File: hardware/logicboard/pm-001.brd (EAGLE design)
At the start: 45 x 45 mm, 18 parts, among them K1 G5V1, T1 2SC1815

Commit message: OSHW logo.
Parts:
- added LOGO1: OSHW-LOGOL-COPPER, SparkFun-Aesthetics:OSHW-LOGO-L_COPPER
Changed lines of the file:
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@@
 <setting verticaltext="up"/>
 </settings>
-<grid distance="50" unitdist="mil" unit="mil" style="lines" multiple="1" display="yes" altdistance="5" altunitdist="mil" altunit="mil"/>
+<grid distance="1" unitdist="mm" unit="mm" style="lines" multiple="1" display="yes" altdistance="5" altunitdist="mil" altunit="mil"/>
 <layers>
 <layer number="1" name="Top" color="4" fill="1" visible="no" active="yes"/>
-<layer number="16" name="Bottom" color="1" fill="1" visible="no" active="yes"/>
+<layer number="16" name="Bottom" color="1" fill="1" visible="yes" active="yes"/>
 <layer number="17" name="Pads" color="2" fill="1" visible="yes" active="yes"/>
 <layer number="18" name="Vias" color="2" fill="1" visible="yes" active="yes"/>
@@
 <attribute name="VALUE" x="36.47" y="43.455" size="1.27" layer="27" rot="R180"/>
 </element>
+<element name="LOGO1" library="SparkFun-Aesthetics" package="OSHW-LOGO-L_COPPER" value="OSHW-LOGOL-COPPER" x="22.5" y="15" rot="MR0"/>
 </elements>
 <signals>

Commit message: Pineapple logo v2.
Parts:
- added U$2: PINEAPPLELOGO2, pineapplelogo2:PINEAPPLELOGO2
- LOGO1: value OSHW-LOGOL-COPPER -> OSHW-LOGOS-COPPER; device SparkFun-Aesthetics:OSHW-LOGO-L_COPPER -> SparkFun-Aesthetics:OSHW-LOGO-S_COPPER
- moved LOGO1 1.12 mm to (22.0, 14.0)
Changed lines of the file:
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@@
 <grid distance="1" unitdist="mm" unit="mm" style="lines" multiple="1" display="yes" altdistance="5" altunitdist="mil" altunit="mil"/>
 <layers>
-<layer number="1" name="Top" color="4" fill="1" visible="no" active="yes"/>
+<layer number="1" name="Top" color="4" fill="1" visible="yes" active="yes"/>
 <layer number="16" name="Bottom" color="1" fill="1" visible="yes" active="yes"/>
 <layer number="17" name="Pads" color="2" fill="1" visible="yes" active="yes"/>
@@
 <attribute name="VALUE" x="36.47" y="43.455" size="1.27" layer="27" rot="R180"/>
 </element>
-<element name="LOGO1" library="SparkFun-Aesthetics" package="OSHW-LOGO-L_COPPER" value="OSHW-LOGOL-COPPER" x="22.5" y="15" rot="MR0"/>
+<element name="U$2" library="pineapplelogo2" package="PINEAPPLELOGO2" value="PINEAPPLELOGO2" x="30" y="12" rot="MR0"/>
+<element name="LOGO1" library="SparkFun-Aesthetics" package="OSHW-LOGO-S_COPPER" value="OSHW-LOGOS-COPPER" x="22" y="14" rot="MR0"/>
 </elements>
 <signals>

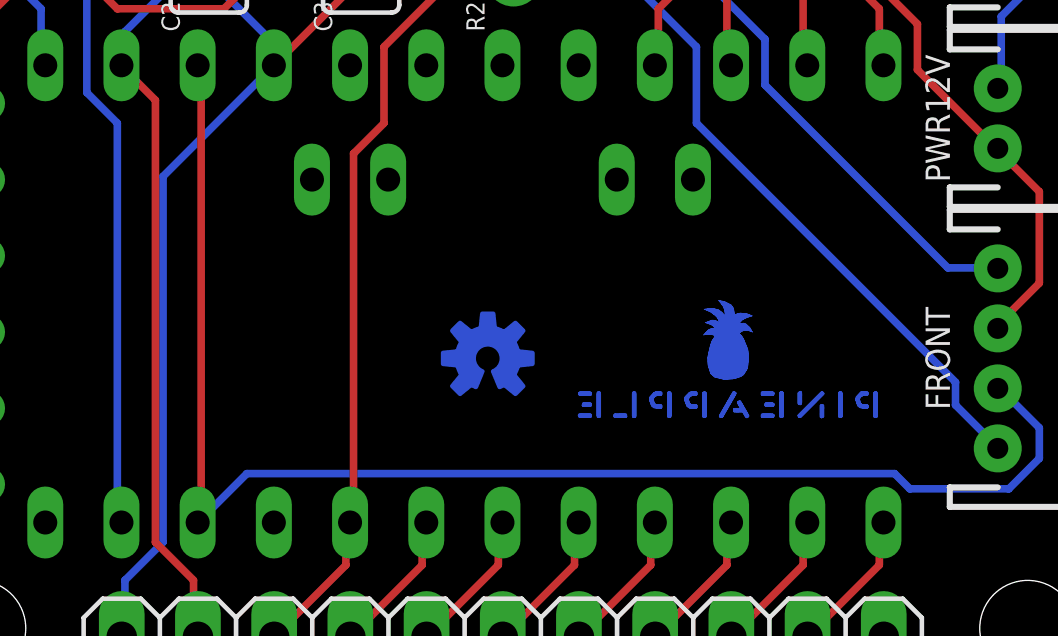
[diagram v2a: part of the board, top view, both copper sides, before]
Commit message: New pineapple logo.
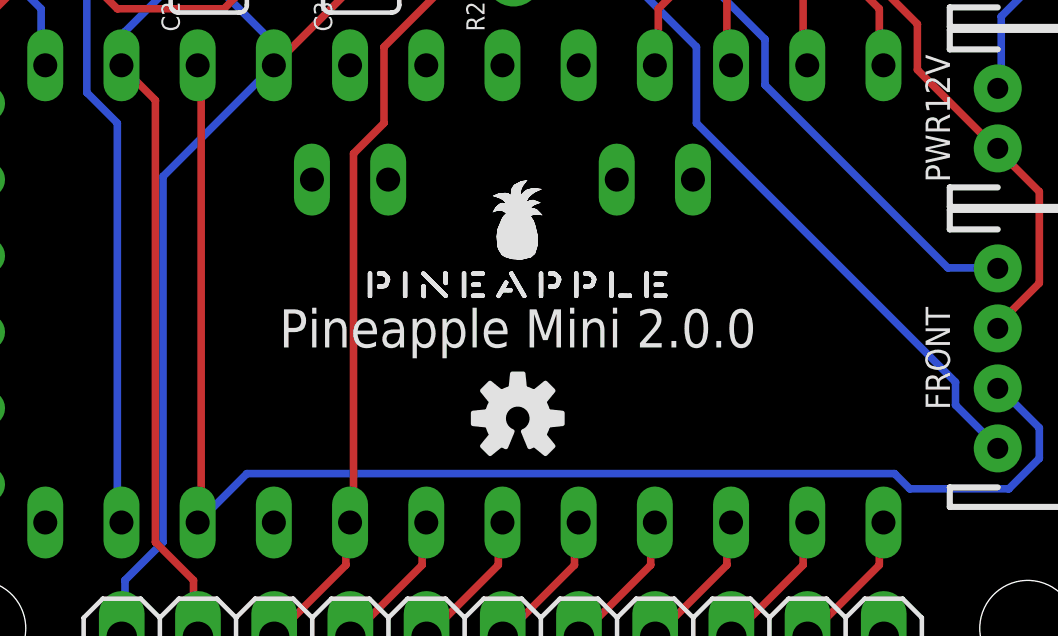
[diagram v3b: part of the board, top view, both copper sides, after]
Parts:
- LOGO1: value OSHW-LOGOS-COPPER -> OSHW-LOGOS; device SparkFun-Aesthetics:OSHW-LOGO-S_COPPER -> SparkFun-Aesthetics:OSHW-LOGO-S
- U$2: value PINEAPPLELOGO2 -> PINEAPPLELOGO2SILKMINI; device pineapplelogo2:PINEAPPLELOGO2 -> pineapplelogo:PINEAPPLELOGO2SILKMINI
- moved U$2 8.06 mm to (23.0, 16.0), flipped to the top
- moved LOGO1 2.24 mm to (23.0, 12.0), flipped to the top
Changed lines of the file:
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@@
 <text x="25.4" y="44.45" size="0.6096" layer="25" rot="R90" align="bottom-right">R11</text>
 <text x="22.86" y="44.45" size="0.6096" layer="25" rot="R90" align="bottom-right">R12</text>
+<text x="23" y="15" size="1.27" layer="21" align="center">Pineapple Mini 2.0.0</text>
 </plain>
 <attributes>
@@
 <attribute name="VALUE" x="36.47" y="43.455" size="1.27" layer="27" rot="R180"/>
 </element>
-<element name="U$2" library="pineapplelogo2" package="PINEAPPLELOGO2" value="PINEAPPLELOGO2" x="30" y="12" rot="MR0"/>
-<element name="LOGO1" library="SparkFun-Aesthetics" package="OSHW-LOGO-S_COPPER" value="OSHW-LOGOS-COPPER" x="22" y="14" rot="MR0"/>
+<element name="U$2" library="pineapplelogo" package="PINEAPPLELOGO2SILKMINI" value="PINEAPPLELOGO2SILKMINI" x="23" y="16"/>
+<element name="LOGO1" library="SparkFun-Aesthetics" package="OSHW-LOGO-S" value="OSHW-LOGOS" x="23" y="12"/>
 </elements>
 <signals>
@@
 <wire x1="33.02" y1="36.83" x2="33.528" y2="36.322" width="0.254" layer="1"/>
 <wire x1="38.862" y1="21.082" x2="39" y2="21" width="0.254" layer="1"/>
-<polygon width="0.254" layer="16">
+<polygon width="0.127" layer="1">
 <vertex x="1" y="1"/>
 <vertex x="44" y="1"/>
@@
 <vertex x="1" y="44"/>
 </polygon>
-<polygon width="0.254" layer="1">
+<polygon width="0.127" layer="16">
 <vertex x="1" y="1"/>
 <vertex x="44" y="1"/>

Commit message: Silk.
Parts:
- moved LOGO1 0.50 mm to (23.0, 12.5)
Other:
- board text added: "Pineapple Mini Rev. 2.0.0"
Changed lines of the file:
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@@
 <hole x="40" y="40" drill="3.2"/>
 <hole x="5" y="40" drill="3.2"/>
-<text x="1" y="43" size="1.27" layer="25">Pineapple Mini 2.0.0</text>
+<text x="1" y="43" size="1.016" layer="25">Pineapple Mini 2.0.0</text>
 <rectangle x1="0" y1="44" x2="45" y2="45" layer="41"/>
 <rectangle x1="44" y1="0" x2="45" y2="45" layer="41"/>
@@
 <text x="25.4" y="44.45" size="0.6096" layer="25" rot="R90" align="bottom-right">R11</text>
 <text x="22.86" y="44.45" size="0.6096" layer="25" rot="R90" align="bottom-right">R12</text>
-<text x="23" y="15" size="1.27" layer="21" align="center">Pineapple Mini 2.0.0</text>
+<text x="23" y="15" size="1.016" layer="21" align="center">Pineapple Mini Rev. 2.0.0</text>
 </plain>
 <attributes>
@@
 </element>
 <element name="U$2" library="pineapplelogo" package="PINEAPPLELOGO2SILKMINI" value="PINEAPPLELOGO2SILKMINI" x="23" y="16"/>
-<element name="LOGO1" library="SparkFun-Aesthetics" package="OSHW-LOGO-S" value="OSHW-LOGOS" x="23" y="12"/>
+<element name="LOGO1" library="SparkFun-Aesthetics" package="OSHW-LOGO-S" value="OSHW-LOGOS" x="23" y="12.5"/>
 </elements>
 <signals>

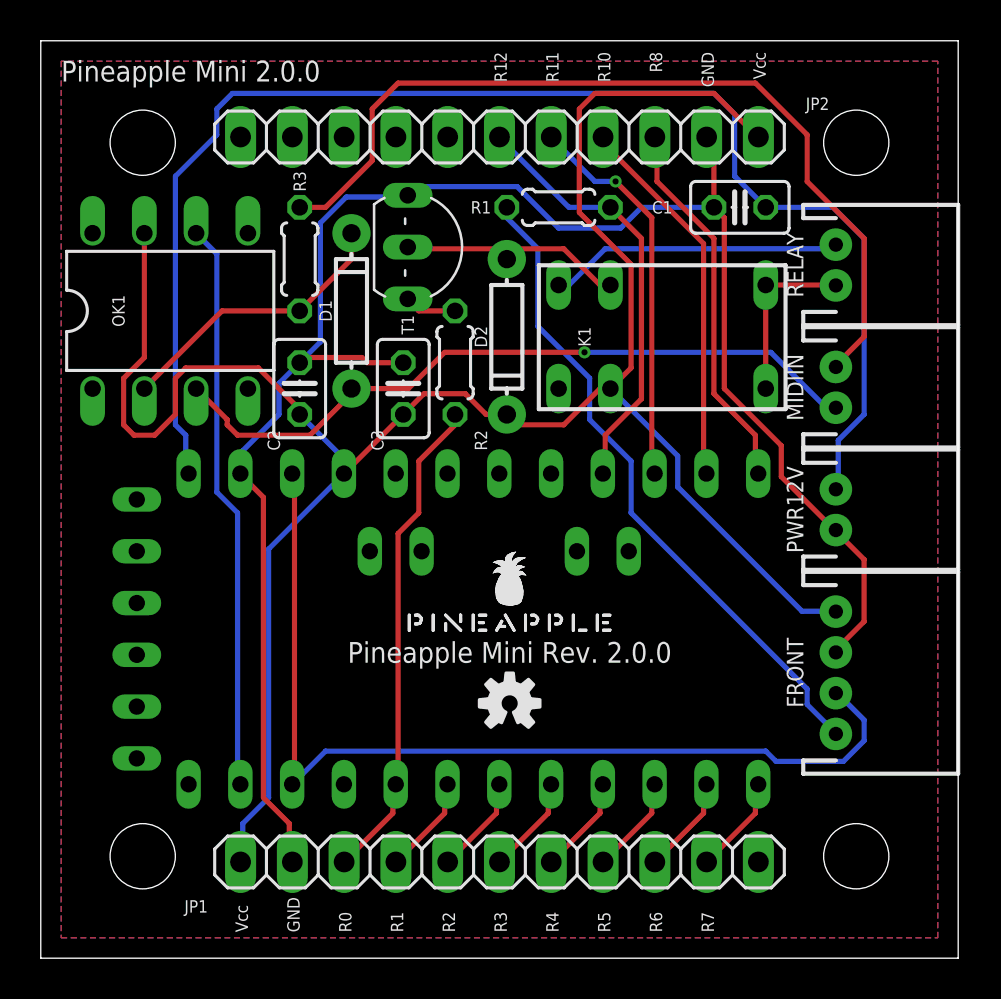
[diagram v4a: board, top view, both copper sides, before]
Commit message: Updated silk patterns and signal names.
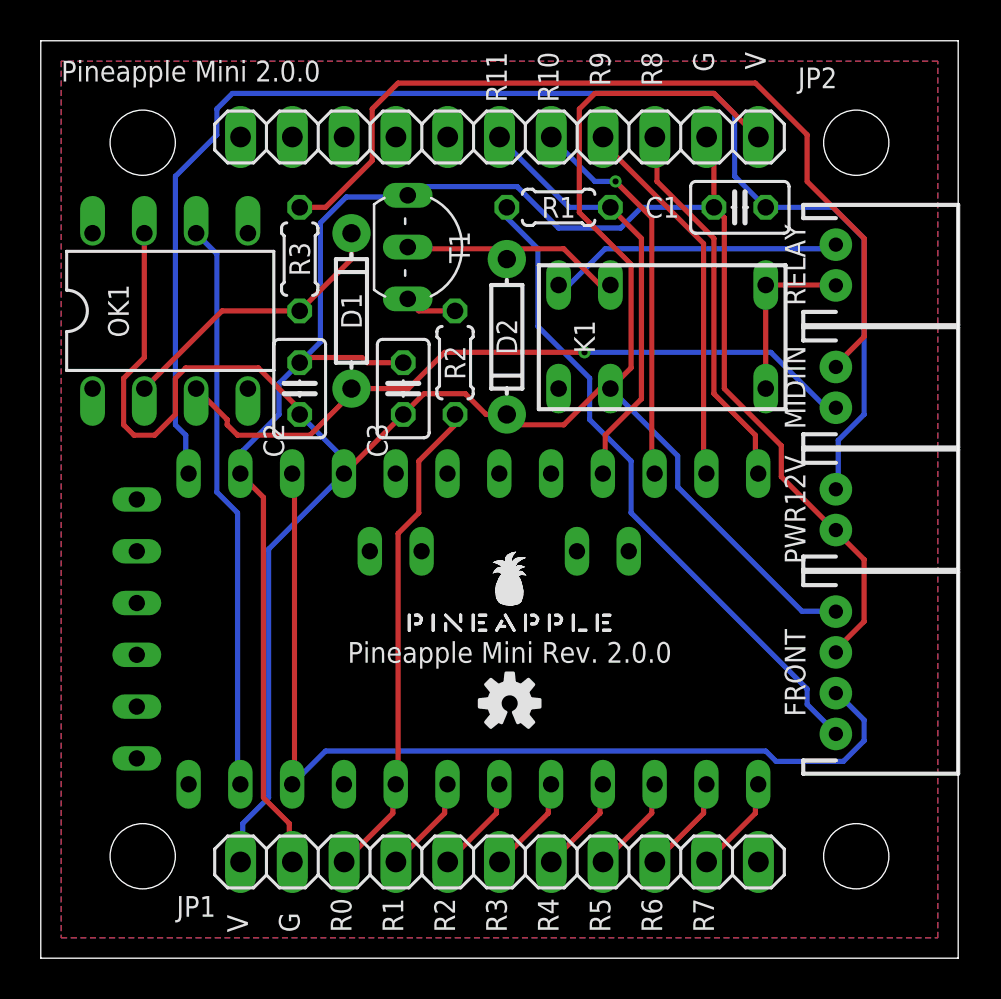
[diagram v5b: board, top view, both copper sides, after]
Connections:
- net N$1 renamed INDR
- net N$10 renamed RELAYB
- net N$11 renamed RELAYA
- net N$2 renamed MIDIIN+
- net N$3 renamed MIDIIN
- net N$5 renamed MIDIIN-
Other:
- board text added: "G"
- board text added: "R9"
- board text added: "V"
- board text removed: "GND"
- board text removed: "R12"
- board text removed: "Vcc"

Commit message: Changed signal names.
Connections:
- net N$4 renamed MIDIINA
- net N$6 renamed 0R
- net N$8 renamed RELAYC
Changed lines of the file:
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@@
 <wire x1="39.116" y1="29.21" x2="39" y2="29" width="0.254" layer="1"/>
 </signal>
-<signal name="N$4">
+<signal name="MIDIINA">
 <contactref element="R3" pad="1"/>
 <contactref element="OK1" pad="2"/>
@@
 <via x="26.67" y="29.718" extent="1-16" drill="0.3"/>
 </signal>
-<signal name="N$6">
+<signal name="0R">
 <contactref element="T1" pad="B"/>
 <contactref element="R2" pad="2"/>
@@
 <wire x1="18.034" y1="32.258" x2="18" y2="32.34" width="0.254" layer="1"/>
 </signal>
-<signal name="N$8">
+<signal name="RELAYC">
 <contactref element="K1" pad="9"/>
 <contactref element="T1" pad="C"/>

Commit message: Pineapple Logo (vector->bitmap), OSHW logo (silk -> copper).
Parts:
- LOGO1: value OSHW-LOGOS -> OSHW-LOGOS-COPPER; device SparkFun-Aesthetics:OSHW-LOGO-S -> SparkFun-Aesthetics:OSHW-LOGO-S_COPPER
- U$2: value PINEAPPLELOGO2SILKMINI -> PINEAPPLE450; device pineapplelogo:PINEAPPLELOGO2SILKMINI -> pineapple:PINEAPPLE450
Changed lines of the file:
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@@
 <attribute name="VALUE" x="36.47" y="43.455" size="1.27" layer="27" rot="R180"/>
 </element>
-<element name="U$2" library="pineapplelogo" package="PINEAPPLELOGO2SILKMINI" value="PINEAPPLELOGO2SILKMINI" x="23" y="16"/>
-<element name="LOGO1" library="SparkFun-Aesthetics" package="OSHW-LOGO-S" value="OSHW-LOGOS" x="23" y="12.5"/>
+<element name="U$2" library="pineapple" package="PINEAPPLE450" value="PINEAPPLE450" x="23" y="16"/>
+<element name="LOGO1" library="SparkFun-Aesthetics" package="OSHW-LOGO-S_COPPER" value="OSHW-LOGOS-COPPER" x="23" y="12.5"/>
 </elements>
 <signals>
